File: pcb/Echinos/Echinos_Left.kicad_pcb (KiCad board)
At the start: 2 copper layers, 167.4 x 138.9 mm, 134 parts, among them J200 USB_B_Micro, J201 Conn_01x04_Socket, J202 Conn_01x12_Socket, J203 Conn_01x06_Socket, J204 Conn_01x06_Socket, J205 Conn_01x06_Socket, J206 USB_C_Receptacle_USB2.0, J207 Conn_01x05_Socket, SW200 SW_Push, SW201 SW_Push, SW202 SW_Push, SW203 SW_Push, SW204 SW_Push, SW205 SW_Push, SW206 SW_Push, SW207 SW_Push, SW208 SW_Push, SW209 SW_Push, SW210 SW_Push, SW211 SW_Push, SW212 SW_Push, SW213 SW_Push, SW214 SW_Push, SW215 SW_Push, SW216 SW_Push, SW217 SW_Push, SW218 SW_Push, SW219 SW_Push, SW220 SW_Push, SW221 SW_Push, SW222 SW_Push, SW223 SW_Push, SW224 Boot, SW225 Boot, SW226 Reset, SW227 Reset, U200 W25Q128JVP, U201 RP2040, U202 USBLC6-2P6, U203 74LVC1T45, U204 USBLC6-2P6, U205 XC6210B332MR-G, Y200 Crystal_GND24

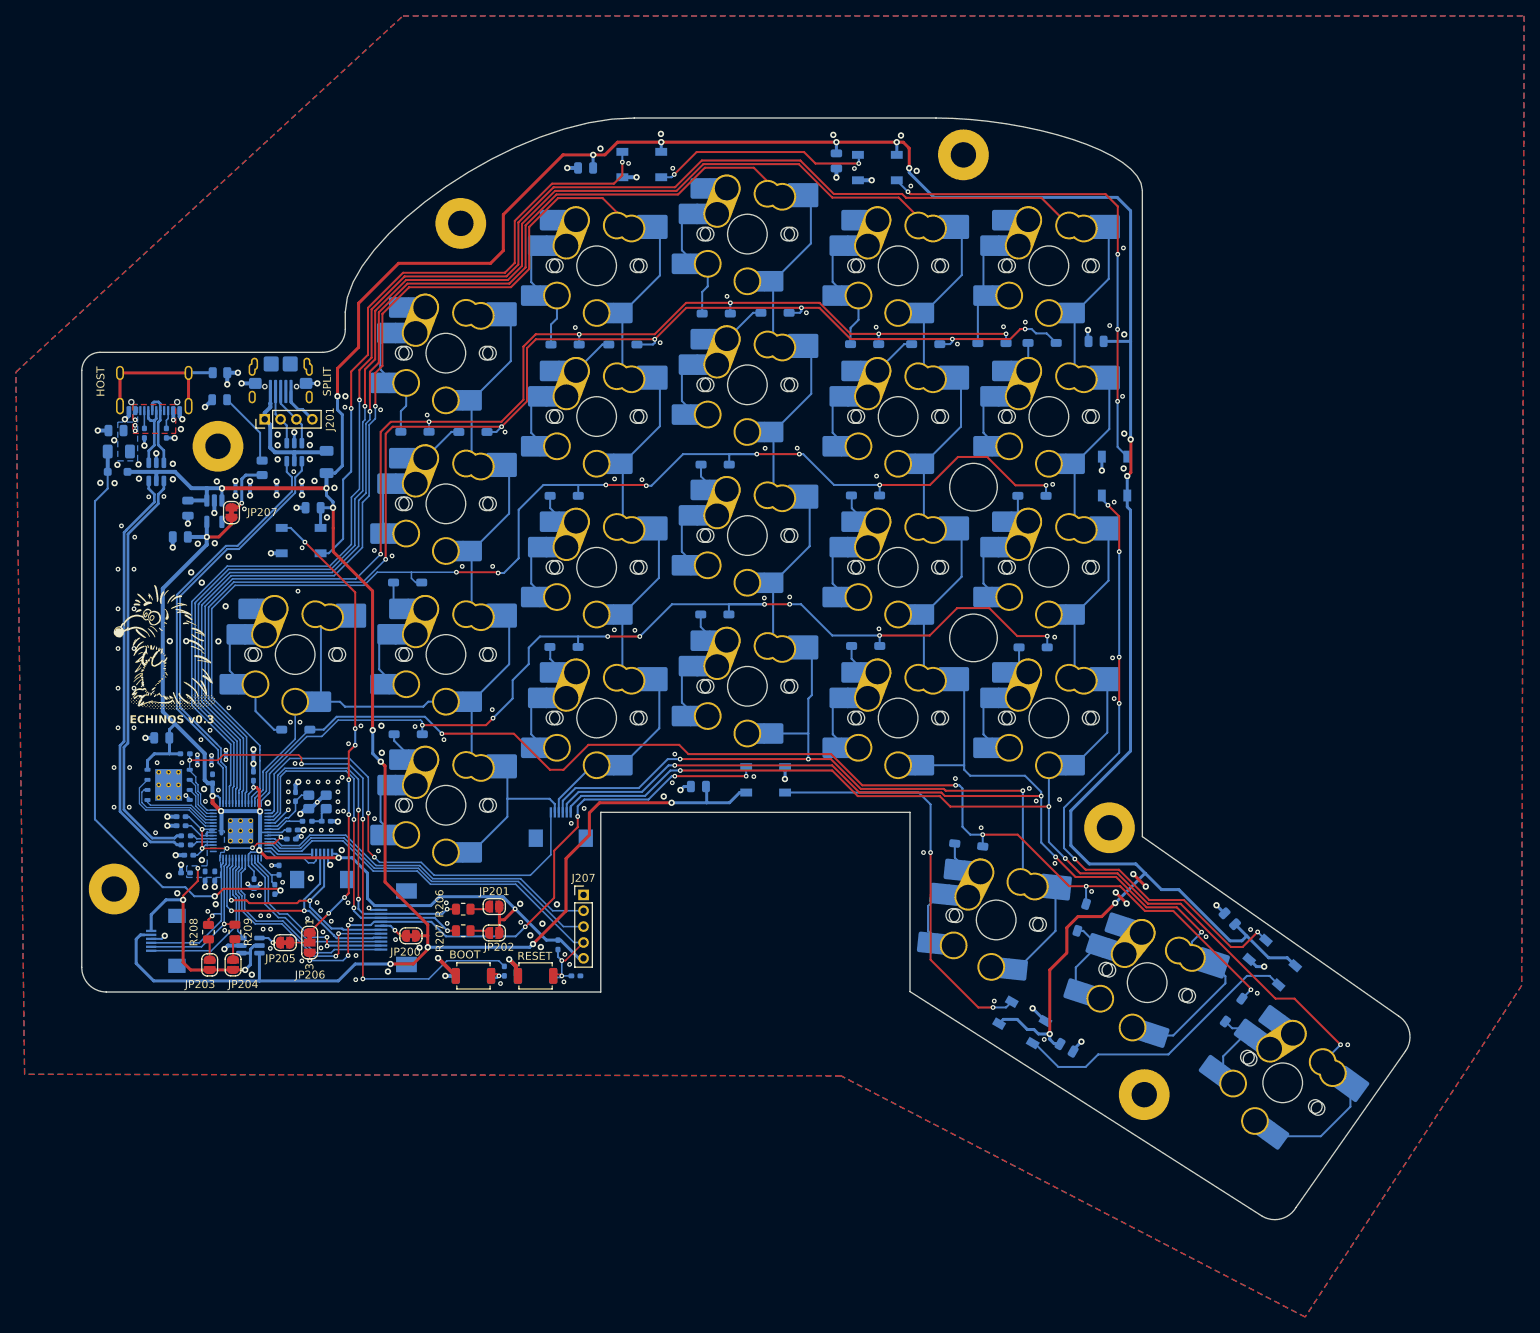
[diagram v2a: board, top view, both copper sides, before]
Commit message: [PCB] - Save last state with on board RP2040.   - Move to kicad 10   - Add DRC custom rule to exclude errors on PTH for switches due to holes being too close   - Move thermal via in both RP2040 and Flash memory to pad corners (better for manufacturing)   - Update USB footprint to match changes in kicad associated symbol   - Increase trackpoint holes from 3.0 to 3.2mm (cannot do more I guess)   - Removed unused footprint from library
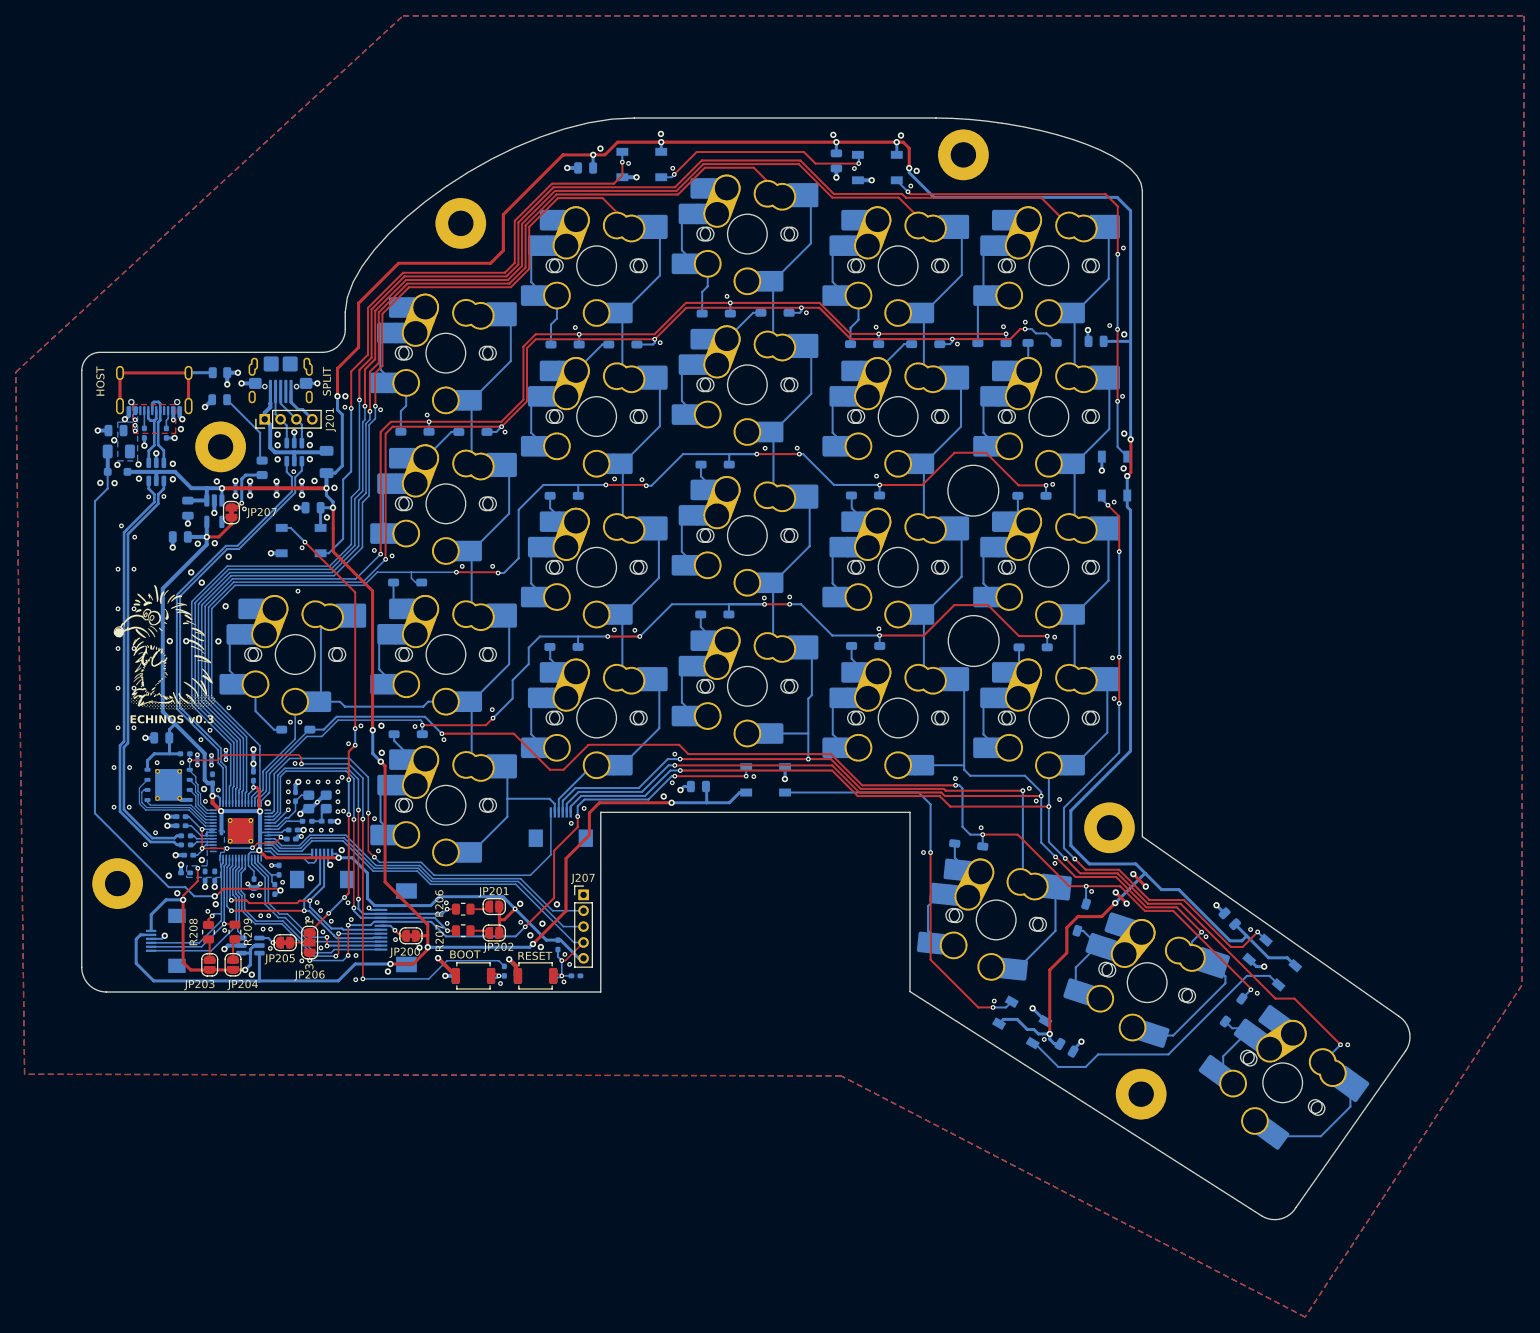
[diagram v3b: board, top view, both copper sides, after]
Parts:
- SW224, SW225: value Boot -> Button
- SW226, SW227: value Reset -> Button
- U201: footprint Echinos:RP2040-QFN-56 -> Echinos:QFN-56-1EP_7x7mm_P0.4mm_EP3.2x3.2mm_ThermalVias
- moved H203 0.81 mm to (50.6, 142.3)
- moved H201 0.39 mm to (179.6, 168.8)
- moved H204 0.34 mm to (63.6, 87.2)
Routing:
- net GND: track 103.6 -> 104.2 mm, vias 272 -> 271
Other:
- outline, holes or cut-outs redrawn
